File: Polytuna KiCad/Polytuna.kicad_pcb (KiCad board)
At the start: 2 copper layers, 0 parts

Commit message: Started PCB
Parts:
- added BOARD1: BOARD_TEENSY_3.1, def-footprints:Board_Teensy_3_1, F.Cu at (224.8, 102.9)
- added BT1: Battery, Pin_Headers:Pin_Header_Straight_1x02_Pitch2.54mm, F.Cu at (237.5, 139.7)
- added C1: C, Capacitors_SMD:C_0805, F.Cu at (156.8, 128.3)
- added C2: 2.2uF, Capacitors_SMD:C_0805, F.Cu at (240.0, 83.8)
- added C3: 2.2uF, Capacitors_SMD:C_0805, F.Cu at (217.2, 85.1)
- added C4: 0.1uF, Capacitors_SMD:C_0805, F.Cu at (217.2, 90.2)
- added C5: 0.1uF, Capacitors_SMD:C_0805, F.Cu at (230.4, 82.8)
- added C6: 2.2uF, Capacitors_SMD:C_0805, F.Cu at (210.8, 85.1)
- added C7: 0.1uF, Capacitors_SMD:C_0805, F.Cu at (221.0, 85.1)
- added C8: 2.2uF, Capacitors_SMD:C_0805, F.Cu at (210.8, 90.2)
- added Ct1: 0.15uF, Capacitors_SMD:C_0805, F.Cu at (240.0, 90.2)
- added D1: LED, LEDs:LED_D3.0mm, F.Cu at (204.5, 135.9)
- added D2: LED, LEDs:LED_D3.0mm, F.Cu at (204.5, 120.7)
- added D3: LED, LEDs:LED_D3.0mm, F.Cu at (204.5, 128.3)
- added Ferrite1: 600, Inductors_SMD:L_0805, F.Cu at (234.9, 90.2)
- added IC1: AP7313-33SAG-7, TO_SOT_Packages_SMD:SOT-23, F.Cu at (234.9, 85.1)
- added Input1: Audio-Jack-2, def-footprints:CONN_Jack_Female_6.35mm_THD, F.Cu at (175.3, 134.6)
- added J1: Barrel_Jack, Connectors:Barrel_Jack_CUI_PJ-102AH, F.Cu at (232.4, 130.8)
- added J2: Conn_01x02, Pin_Headers:Pin_Header_Straight_1x02_Pitch2.54mm, F.Cu at (133.3, 142.2)
- added J3: Conn_01x02, Pin_Headers:Pin_Header_Straight_1x02_Pitch2.54mm, F.Cu at (147.3, 142.2)
- added J4: Conn_01x04, Pin_Headers:Pin_Header_Straight_1x04_Pitch2.54mm, F.Cu at (226.1, 120.7)
- added JMP1: 2Jumper, def-footprints:Miscellaneous_Solder_Jumper, F.Cu at (154.9, 96.5)
- added Output1: Audio-Jack-2, def-footprints:CONN_Jack_Female_6.35mm_THD, F.Cu at (175.3, 95.2)
- added R1: R, Resistors_SMD:R_0805, F.Cu at (133.3, 105.4)
- added R10: 10M, Resistors_SMD:R_0805, F.Cu at (160.0, 96.5)
- added R2: R, Resistors_SMD:R_0805, F.Cu at (151.4, 128.1)
- added R3: R, Resistors_SMD:R_0805, F.Cu at (144.9, 127.5)
- added R4: R, Resistors_SMD:R_0805, F.Cu at (163.1, 121.9)
- added R5: R, Resistors_SMD:R_0805, F.Cu at (162.6, 117.9)
- added R6: R, Resistors_SMD:R_0805, F.Cu at (162.6, 114.3)
- added R7: R, Resistors_SMD:R_0805, F.Cu at (163.1, 110.2)
- added R8: 2.2K, Resistors_SMD:R_0805, F.Cu at (205.7, 83.8)
- added R9: 2.2K, Resistors_SMD:R_0805, F.Cu at (221.0, 91.4)
- added RV1: POT_TRIM, Potentiometers:Potentiometer_Alps_RK09K_Horizontal, F.Cu at (188.0, 96.5)
- added RV2: POT_TRIM, Potentiometers:Potentiometer_Alps_RK09K_Horizontal, F.Cu at (188.0, 132.1)
- added RV3: POT_TRIM, Potentiometers:Potentiometer_Alps_RK09K_Horizontal, F.Cu at (188.0, 114.3)
- added SW1: SW_Push, Buttons_Switches_THT:SW_PUSH_6mm_h5mm, F.Cu at (133.3, 83.8)
- added SW2: SW_Push, Buttons_Switches_THT:SW_PUSH_6mm_h5mm, F.Cu at (147.3, 83.8)
- added SW3: SW_Push, Buttons_Switches_THT:SW_PUSH_6mm_h5mm, F.Cu at (133.2, 93.6)
- added SW4: SW_DPDT_x2, def-footprints:Switches_Stomp_Switch_3PDT, F.Cu at (148.6, 111.8)
- added U1: LM358, Housings_SOIC:SOIC-8-1EP_3.9x4.9mm_Pitch1.27mm, F.Cu at (172.7, 114.3)
- added U2: SGTL5000, Housings_DFN_QFN:QFN-32-1EP_5x5mm_Pitch0.5mm, F.Cu at (228.2, 88.1)
- added U3: L7805, TO_SOT_Packages_THT:TO-220-3_Horizontal, F.Cu at (228.6, 141.0)
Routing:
- net +3V3: track 0.00 -> 24.4 mm
- net Net-(BT1-Pad1): track 0.00 -> 22.8 mm
- net GND: track 0.00 -> 15.2 mm
- net Net-(R6-Pad1): track 0.00 -> 10.9 mm
- net GNDA: track 0.00 -> 9.15 mm
- net Net-(C2-Pad2): track 0.00 -> 6.90 mm
- net Net-(C1-Pad1): track 0.00 -> 3.30 mm
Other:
- board outline added: 114.3 x 63.5 mm

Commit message: Progress in routing
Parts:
- C3, C4, C5, C6, Ct1, D1, D2, D3, IC1, RV1, RV2, RV3, SW1, SW2, SW3: moved to B.Cu
- moved R1 61.9 mm to (193.5, 119.9), turned to 180 degrees
- moved R3 52.8 mm to (193.8, 107.7), turned to 180 degrees
- moved R2 44.9 mm to (193.8, 113.5), turned to 180 degrees
- moved R8 42.2 mm to (232.9, 116.1), turned to 180 degrees
- moved D1 33.6 mm to (186.2, 107.7)
- moved C2 31.6 mm to (211.3, 97.0), turned to 270 degrees
- moved R5 27.3 mm to (141.0, 134.6)
- moved R4 27.3 mm to (141.5, 138.7)
- moved R6 27.3 mm to (141.0, 131.1)
- moved R7 27.3 mm to (141.5, 127.0)
- moved U1 27.3 mm to (151.1, 131.1)
- moved SW3 27.1 mm to (160.3, 92.7), turned to 90 degrees
- moved C8 26.2 mm to (236.7, 86.1)
- moved C4 25.6 mm to (240.5, 100.6)
- moved C3 24.9 mm to (240.5, 93.7)
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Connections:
- R1 pad 1: Net-(BOARD1-Pad7) -> Net-(BOARD1-Pad10)
- R2 pad 1: Net-(BOARD1-Pad6) -> Net-(BOARD1-Pad9)
- R3 pad 1: Net-(BOARD1-Pad5) -> Net-(BOARD1-Pad8)
- SW1 pad 2: Net-(BOARD1-Pad2) -> Net-(BOARD1-Pad5)
- SW2 pad 2: Net-(BOARD1-Pad3) -> Net-(BOARD1-Pad6)
- SW3 pad 2: Net-(BOARD1-Pad4) -> Net-(BOARD1-Pad7)
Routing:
- net +3V3: track 24.4 -> 236.6 mm, vias 0 -> 2
- net Net-(BOARD1-Pad5): track 0.00 -> 111.9 mm
- net Net-(BOARD1-Pad6): track 0.00 -> 98.3 mm
- net SGTL_Out: track 0.00 -> 93.1 mm, vias 0 -> 2
- net Net-(BOARD1-Pad7): track 0.00 -> 84.1 mm
- net GND: track 15.2 -> 79.4 mm, vias 0 -> 3
- net Net-(BOARD1-Pad16): track 0.00 -> 59.2 mm
- net Net-(BOARD1-Pad10): track 0.00 -> 56.7 mm, vias 0 -> 2
- net Net-(BOARD1-Pad8): track 0.00 -> 54.8 mm, vias 0 -> 2
- net Net-(BOARD1-Pad9): track 0.00 -> 54.4 mm, vias 0 -> 2
- net Net-(BOARD1-Pad18): track 0.00 -> 46.8 mm
- net Net-(BOARD1-Pad17): track 0.00 -> 46.5 mm
- net SDA: track 0.00 -> 35.0 mm, vias 0 -> 1
- net Net-(C7-Pad1): track 0.00 -> 33.3 mm, vias 0 -> 2
- net Net-(C1-Pad1): track 3.30 -> 32.2 mm, vias 0 -> 2
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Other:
- board size 114.3 x 63.5 mm -> 114.3 x 64.8 mm

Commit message: Moar routing
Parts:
- moved J2 25.4 mm to (158.8, 142.2)
- moved J3 14.7 mm to (171.7, 142.2)
- moved C1 2.50 mm to (135.4, 126.0), turned to 90 degrees
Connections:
- U2 pad 33: Net-(U2-Pad33) -> GND
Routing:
- net GNDA: track 37.1 -> 193.1 mm, vias 2 -> 6
- net Net-(J1-Pad2): track 0.00 -> 113.2 mm
- net GND: track 79.4 -> 185.0 mm, vias 3 -> 10
- net +5V: track 0.00 -> 105.1 mm
- net Net-(SW4-Pad6): track 0.00 -> 97.3 mm, vias 0 -> 2
- net Net-(C1-Pad2): track 0.04 -> 25.0 mm, vias 0 -> 2
- net +3V3: track 236.6 -> 221.0 mm, vias 2 -> 10
- net Net-(JMP1-Pad2): track 0.00 -> 9.93 mm
- net SCL: track 28.8 -> 34.5 mm
- net Net-(BT1-Pad1): track 19.1 -> 21.9 mm, vias 0 -> 2
- net Net-(C1-Pad1): track 32.2 -> 33.5 mm
- net Net-(BOARD1-Pad17): track 46.5 -> 47.0 mm, vias 0 -> 1
- net Net-(BOARD1-Pad16): track 59.2 -> 59.4 mm, vias 0 -> 1
- net Net-(BOARD1-Pad18): track 46.8 -> 47.1 mm, vias 0 -> 1
- net Net-(BOARD1-Pad8): vias 2 -> 0
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- added copper zone on B.Cu, net +3V3
- added copper zone on F.Cu, net +5V
- added copper zone on B.Cu, net GND
- added copper zone on F.Cu, net GND
- added copper zone on B.Cu, net GNDA

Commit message: Moar routing x2
Still have to add the 3pdt
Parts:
- Input1, Output1: value Audio-Jack-2 -> JACK_FEMALE_STEREO_6_PINS
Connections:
- Input1 pad R: (no net) -> GNDA
- Input1 pad RS: (no net) -> GNDA
- Input1 pad S: (no net) -> GNDA
- Input1 pad SS: (no net) -> GNDA
- Input1 pad T: (no net) -> Net-(Input1-PadT)
- Input1 pad TS: (no net) -> GNDA
- Output1 pad R: (no net) -> GNDA
- Output1 pad RS: (no net) -> GNDA
- Output1 pad S: (no net) -> GNDA
- Output1 pad SS: (no net) -> GNDA
- Output1 pad T: (no net) -> Net-(JMP1-Pad2)
- Output1 pad TS: (no net) -> GNDA
- SW4 pad 2: Net-(Input1-Pad1) -> Net-(Input1-PadT)
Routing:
- net +3V3: track 221.0 -> 35.7 mm, vias 10 -> 5
- net GNDA: track 193.1 -> 53.1 mm, vias 6 -> 7
- net Net-(C2-Pad2): track 6.90 -> 84.0 mm, vias 0 -> 4
- net Net-(Input1-PadT): track 0.00 -> 62.2 mm, vias 0 -> 2
- net Net-(JMP1-Pad2): track 9.93 -> 45.4 mm, vias 0 -> 1
- net GND: track 185.0 -> 156.7 mm, vias 10 -> 8
- net (no net): track 0.00 -> 8.25 mm
- net SGTL_Out: track 93.1 -> 94.1 mm, vias 2 -> 4
- net LineIN(SGTL): track 13.4 -> 14.2 mm
- net Pin11_Teensy: vias 0 -> 2
- added copper zone on F.Cu, net +3V3
- removed copper zone on B.Cu, net +3V3

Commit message: PCB v0.1
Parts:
- added LED_SW: Conn_01x02, Pin_Headers:Pin_Header_Straight_1x02_Pitch2.54mm, F.Cu at (137.9, 110.5)
- BOARD1: value BOARD_TEENSY_3.1 -> BOARD_TEENSY_3.X
- SW4: value SW_DPDT_x2 -> SW_TPDT; footprint def-footprints:Switches_Stomp_Switch_3PDT -> footprints:IceStomp_Switch_3PDT
- moved Display 1.27 mm to (239.3, 112.5)
- moved D1 0.76 mm to (186.2, 106.9)
- moved D3 0.76 mm to (186.2, 119.1)
- moved R1 0.76 mm to (193.5, 119.1)
- moved R3 0.76 mm to (193.8, 106.9)
- moved D2 0.51 mm to (186.2, 113.0)
- moved R2 0.51 mm to (193.8, 113.0)
- renumbered J2 to +3.3V, J3 to +5V, J4 to Display
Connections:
- BOARD1 pad 12: Net-(BOARD1-Pad12) -> (no net)
- BOARD1 pad 14: Net-(BOARD1-Pad14) -> (no net)
- BOARD1 pad 19: Net-(BOARD1-Pad19) -> (no net)
- BOARD1 pad 2: Net-(BOARD1-Pad2) -> (no net)
- BOARD1 pad 22: Net-(BOARD1-Pad22) -> (no net)
- BOARD1 pad 23: Net-(BOARD1-Pad23) -> (no net)
- BOARD1 pad 3: Net-(BOARD1-Pad3) -> (no net)
- BOARD1 pad 4: Net-(BOARD1-Pad4) -> (no net)
- C1 pad 2: Net-(C1-Pad2) -> InputStage
- Input1 pad T: Net-(Input1-PadT) -> INPUT
- J1 pad 2: Net-(J1-Pad2) -> PowerIn
- JMP1 pad 2: Net-(JMP1-Pad2) -> Output
- Output1 pad T: Net-(JMP1-Pad2) -> Output
- U2 pad 11: Net-(U2-Pad11) -> (no net)
- U2 pad 13: Net-(U2-Pad13) -> (no net)
- U2 pad 15: Net-(U2-Pad15) -> (no net)
- U2 pad 16: Net-(U2-Pad16) -> (no net)
- U2 pad 18: Net-(U2-Pad18) -> (no net)
- U2 pad 2: Net-(U2-Pad2) -> (no net)
- U2 pad 4: Net-(U2-Pad4) -> (no net)
- U2 pad 6: Net-(U2-Pad6) -> (no net)
- U3 pad 1: Net-(SW4-Pad6) -> DC_Conv
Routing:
- net DC_Conv: track 0.00 -> 134.1 mm, vias 0 -> 2
- net Net-(J1-Pad2): track 113.2 -> 0.00 mm
- net PowerIn: track 0.00 -> 113.2 mm
- net +5V: track 105.1 -> 5.80 mm
- net Net-(SW4-Pad6): track 97.3 -> 0.00 mm, vias 2 -> 0
- net INPUT: track 0.00 -> 72.5 mm, vias 0 -> 2
- net Net-(Input1-PadT): track 62.2 -> 0.00 mm, vias 2 -> 0
- net Output: track 0.00 -> 45.4 mm, vias 0 -> 1
- net Net-(JMP1-Pad2): track 45.4 -> 0.00 mm, vias 1 -> 0
- net InputStage: track 0.00 -> 27.4 mm
- net Net-(C1-Pad2): track 25.0 -> 0.00 mm, vias 2 -> 0
- net Net-(J5-Pad2): track 0.00 -> 8.40 mm
- net +3V3: track 35.7 -> 39.4 mm
- net (no net): track 8.25 -> 4.95 mm
- net Net-(C2-Pad2): track 84.0 -> 85.6 mm, vias 4 -> 6
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
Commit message: PCB v0.1
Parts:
- moved Ct1 18.9 mm to (235.7, 100.6)
- moved R9 2.29 mm to (230.6, 110.7)
- moved R8 2.03 mm to (230.9, 116.1)
- moved IC1 1.27 mm to (234.4, 95.8)
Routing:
- net PowerIn: track 113.2 -> 144.9 mm
- net GNDA: track 53.1 -> 31.2 mm, vias 7 -> 5
- net Net-(BT1-Pad1): track 21.9 -> 36.5 mm
- net DC_Conv: track 134.1 -> 147.2 mm
- net +3V3: track 39.4 -> 50.2 mm, vias 5 -> 4
- net GND: track 156.7 -> 148.9 mm
- net (no net): track 4.95 -> 0.38 mm
- net Net-(Ct1-Pad1): track 14.0 -> 17.9 mm
- net +5V: track 5.80 -> 2.54 mm
- net SCL: track 33.0 -> 30.7 mm
- net SDA: track 34.2 -> 32.2 mm
- net INPUT: track 72.5 -> 72.0 mm
- net SGTL_Out: track 94.1 -> 94.4 mm, vias 6 -> 4
- net Net-(BOARD1-Pad6): track 98.3 -> 98.5 mm, vias 0 -> 2
- net Net-(BOARD1-Pad8): vias 0 -> 2
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- removed copper zone on F.Cu, net GND
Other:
- net class Power added: clearance 0.2, trace_width 0.5, via_dia 0.6, via_drill 0.4
- board text added: "+"
- board text added: "-"
- board text added: "3V3"
- board text added: "5V"
- board text added: ">"
- board text added: "GND"
- board text added: "SCL"
- board text added: "SDA"
- board text added: "USB"

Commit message: PCB v0.1
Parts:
- removed +3.3V, +5V, LED_SW: Conn_01x02, Pin_Headers:Pin_Header_Straight_1x02_Pitch2.54mm
- removed Display: Conn_01x04, Pin_Headers:Pin_Header_Straight_1x04_Pitch2.54mm
- added J2: Conn_01x02, Pin_Headers:Pin_Header_Straight_1x02_Pitch2.54mm, F.Cu at (158.8, 142.2)
- added J3: Conn_01x02, Pin_Headers:Pin_Header_Straight_1x02_Pitch2.54mm, F.Cu at (171.7, 142.2)
- added J4: Conn_01x04, Pin_Headers:Pin_Header_Straight_1x04_Pitch2.54mm, F.Cu at (239.3, 112.5)
- added J5: Conn_01x02, Pin_Headers:Pin_Header_Straight_1x02_Pitch2.54mm, F.Cu at (137.9, 110.5)
- added JMP2: 2Jumper, def-footprints:Miscellaneous_Solder_Jumper, B.Cu at (217.9, 113.8)
- BOARD1: value BOARD_TEENSY_3.X -> BOARD_TEENSY_3.1
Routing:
- net GND: track 148.9 -> 160.3 mm
- net GNDA: track 31.2 -> 39.7 mm

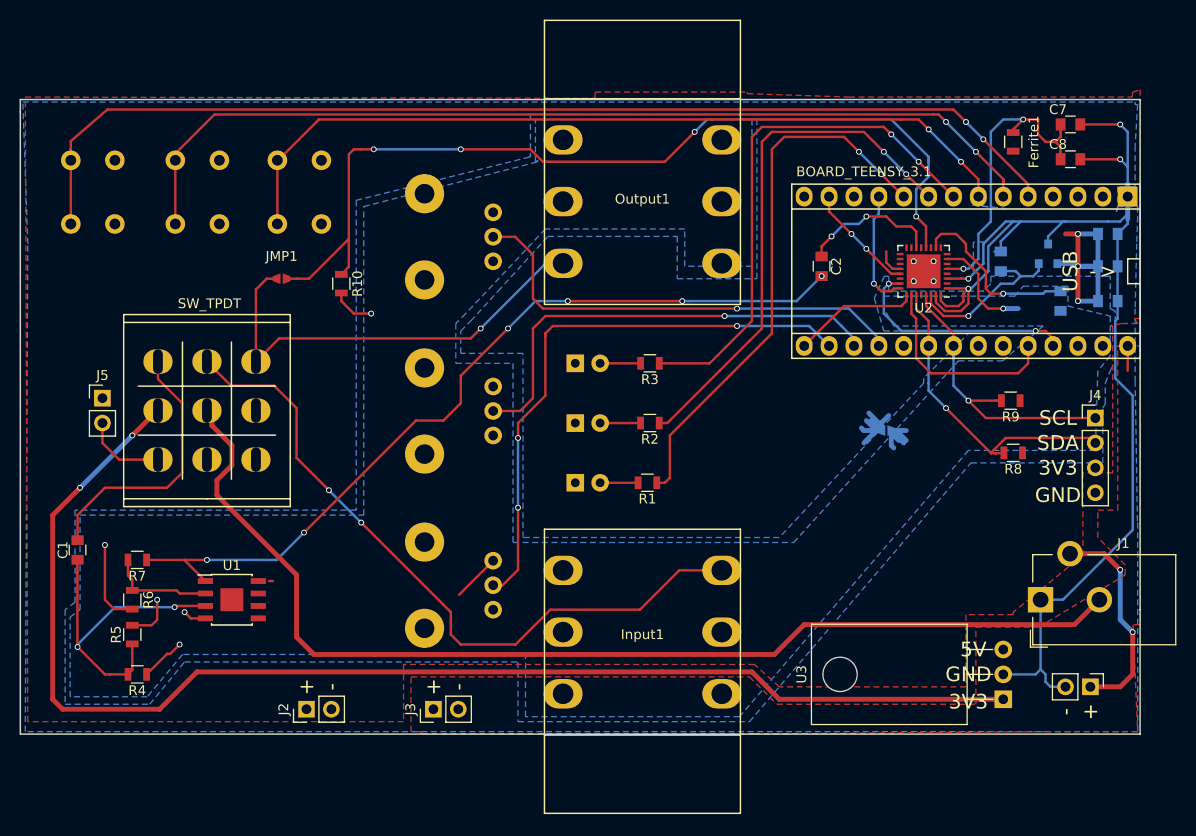
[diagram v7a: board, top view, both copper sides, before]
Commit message: Added some logos and changed silks
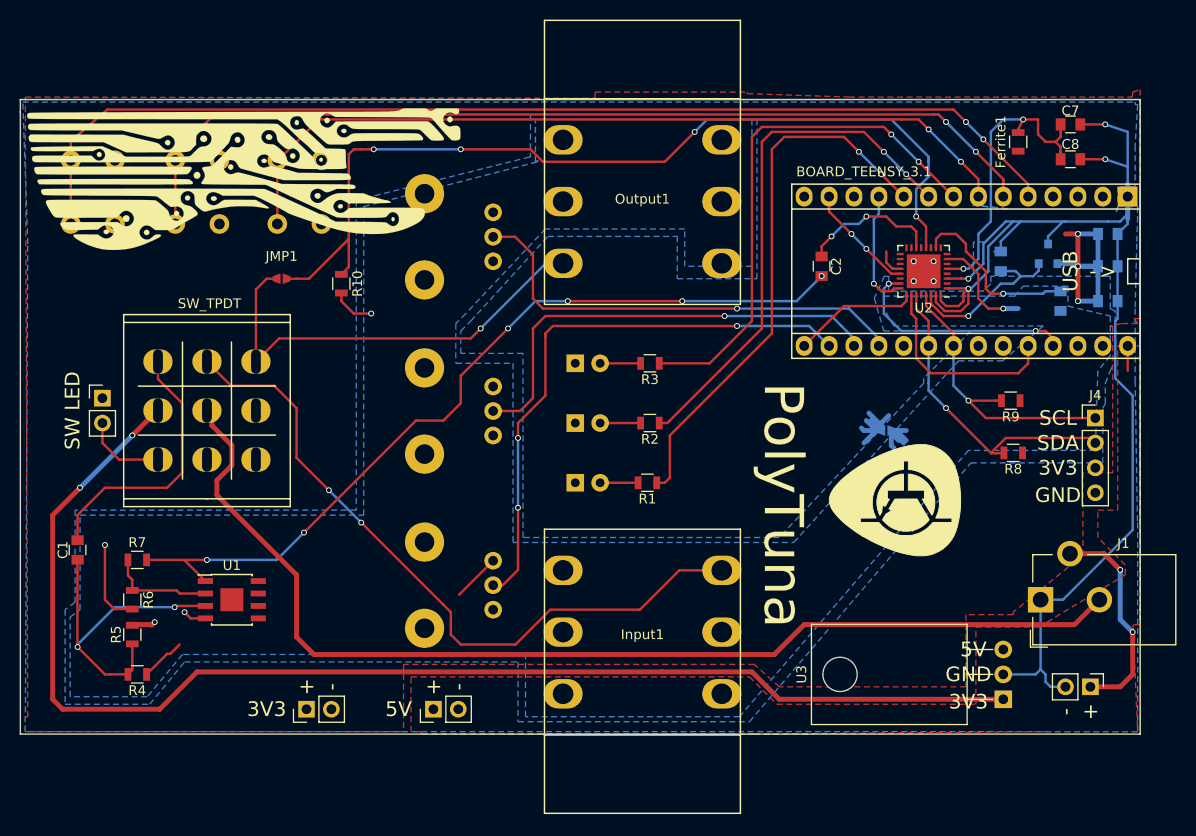
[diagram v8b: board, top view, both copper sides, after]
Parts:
- added G***: LOGO, uc3music_logos:logo_guitar_45x15.4mm, F.Cu at (152.1, 88.6)
- added G***: LOGO, uc3music_logos:logo_pick_15x15mm, F.Cu at (218.8, 120.9)
- moved Ferrite1 0.51 mm to (231.4, 84.3)
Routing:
- net +3V3: vias 4 -> 3
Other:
- board text added: "PolyTuna"
- board text added: "SW LED"
